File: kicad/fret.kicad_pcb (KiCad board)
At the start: 2 copper layers, 40 parts, among them J1 +5V, J10 CONN_01X06, J2 GNDPWR, J3 +3.3V, J4 GND, J5 SDA, J6 SCL, J7 TEST, J8 ~RST, P0 TOUCH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

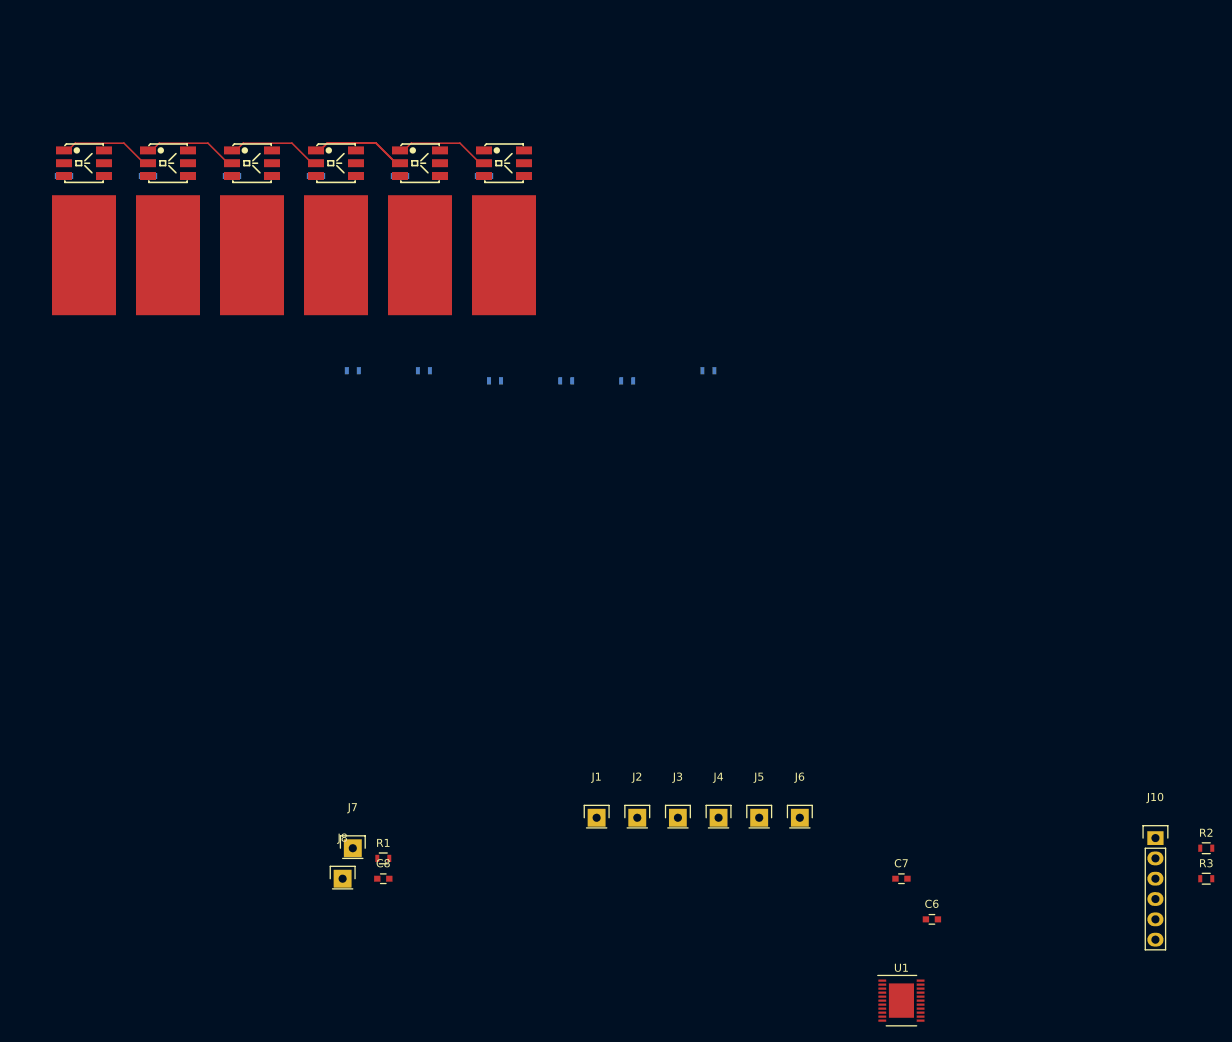
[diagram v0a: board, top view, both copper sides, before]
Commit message: kicad: almost finished layout with the msp430
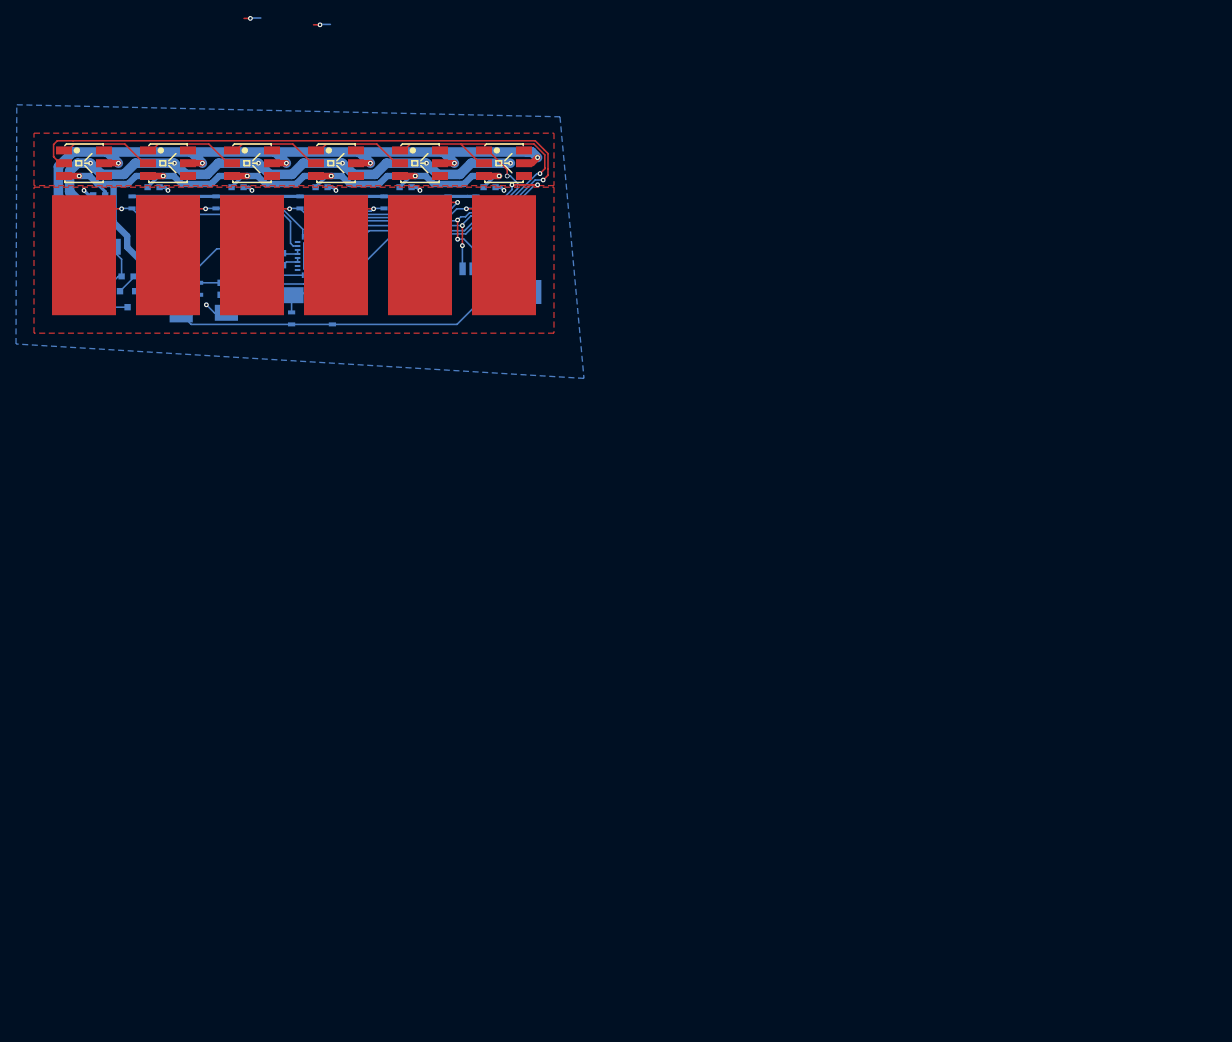
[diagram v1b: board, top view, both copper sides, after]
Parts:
- added C10: 22uF, Capacitors_SMD:C_0805, B.Cu at (44.7, 50.8)
- added C9: 22uF, Capacitors_SMD:C_0805, B.Cu at (38.7, 50.8)
- added JP1: GNDPWR-GND, Capacitors_SMD:C_0603, B.Cu at (41.7, 47.9)
- added U2: AP2210N-3.3TRG1, Housings_SOT-23_SOT-143_TSOT-6:SOT-23, B.Cu at (41.7, 50.8)
- C6, C7, C8, R1, R2, R3: moved to B.Cu
- J1, J2, J3, J4, J5, J6: footprint Pin_Headers:Pin_Header_Straight_1x01 -> guitar-components:IDC-1x1; moved to B.Cu
- J10: footprint Pin_Headers:Pin_Header_Straight_1x06 -> Connectors_Molex:Connector_Molex_PicoBlade_53261-0671; moved to B.Cu
- J7, J8: footprint Pin_Headers:Pin_Header_Straight_1x01 -> guitar-components:pad-2mm-round; moved to B.Cu
- U1: footprint Housings_DFN_QFN:DFN-22-1EP_5x6mm_Pitch0.5mm -> Housings_DFN_QFN:QFN-32-1EP_5x5mm_Pitch0.5mm; moved to B.Cu
- moved R2 132.1 mm to (62.2, 53.1), turned to 90 degrees
- moved R3 129.8 mm to (67.3, 53.1), turned to 90 degrees
- moved U1 118.3 mm to (65.3, 45.4), turned to 270 degrees
- moved C6 115.7 mm to (61.1, 45.8), turned to 270 degrees
- moved C7 110.5 mm to (59.5, 45.8), turned to 270 degrees
- moved J10 107.8 mm to (86.7, 49.9), turned to 180 degrees
- moved J2 97.2 mm to (39.4, 44.2)
- moved J1 96.8 mm to (35.0, 44.2)
- moved J3 88.4 mm to (48.4, 52.6)
- moved J4 88.1 mm to (54.0, 52.5)
- moved J6 87.7 mm to (67.2, 50.2)
- moved J5 87.6 mm to (62.2, 50.2)
- moved C8 76.5 mm to (53.3, 49.5), turned to 270 degrees
- moved J8 75.5 mm to (55.3, 48.9)
- moved R1 74.8 mm to (50.7, 49.5), turned to 270 degrees
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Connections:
- U1 pad 10: /LED6 -> /BUTTON
- U1 pad 13: Net-(U1-Pad13) -> /LED0
- U1 pad 14: /BUTTON -> Net-(U1-Pad14)
- U1 pad 9: /LED0 -> /LED6
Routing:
- net +3V3: track 0.00 -> 171.8 mm, vias 0 -> 6
- net +5V: track 0.00 -> 104.8 mm, vias 0 -> 6
- net /LED0: track 0.00 -> 99.3 mm, vias 0 -> 1
- net /CAOUT: track 0.00 -> 85.0 mm, vias 0 -> 2
- net GNDPWR: track 0.00 -> 80.2 mm, vias 0 -> 6
- net /BUTTON: track 11.9 -> 60.2 mm, vias 0 -> 3
- net /LED6: track 0.00 -> 39.8 mm, vias 0 -> 3
- net Net-(P4-Pad1): track 0.00 -> 32.1 mm, vias 0 -> 1
- net Net-(P5-Pad1): track 0.00 -> 30.4 mm, vias 0 -> 1
- net Net-(P0-Pad1): track 0.00 -> 26.4 mm, vias 0 -> 1
- net GND: track 0.00 -> 17.0 mm, vias 0 -> 7
- net Net-(P1-Pad1): track 0.00 -> 15.0 mm, vias 0 -> 1
- net /~RST: track 0.00 -> 14.4 mm
- net Net-(P3-Pad1): track 0.00 -> 12.3 mm, vias 0 -> 1
- net /LED4: track 23.8 -> 12.3 mm
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- added copper zone on B.Cu, net GND
- added copper zone on F.Cu, net GND
- added copper zone on F.Cu, net GNDPWR

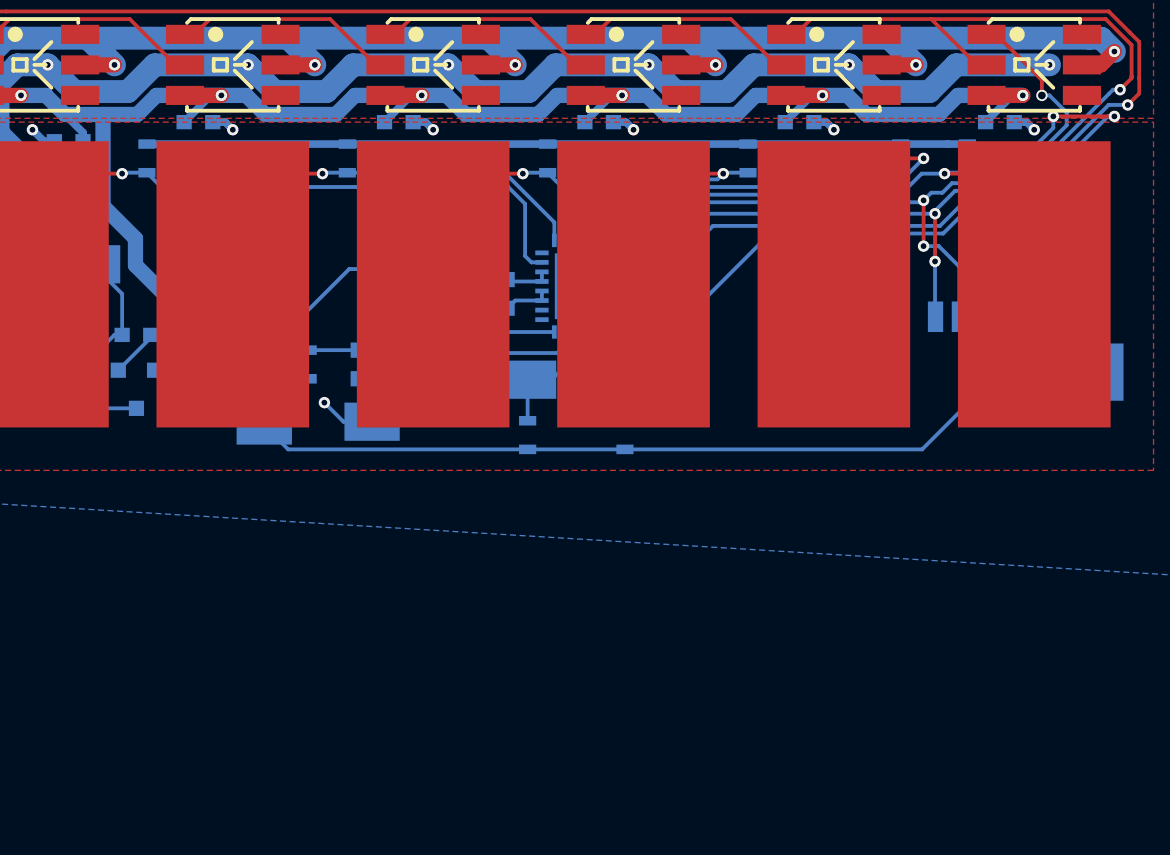
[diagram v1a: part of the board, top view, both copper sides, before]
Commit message: kicad: started fret layout with stm32
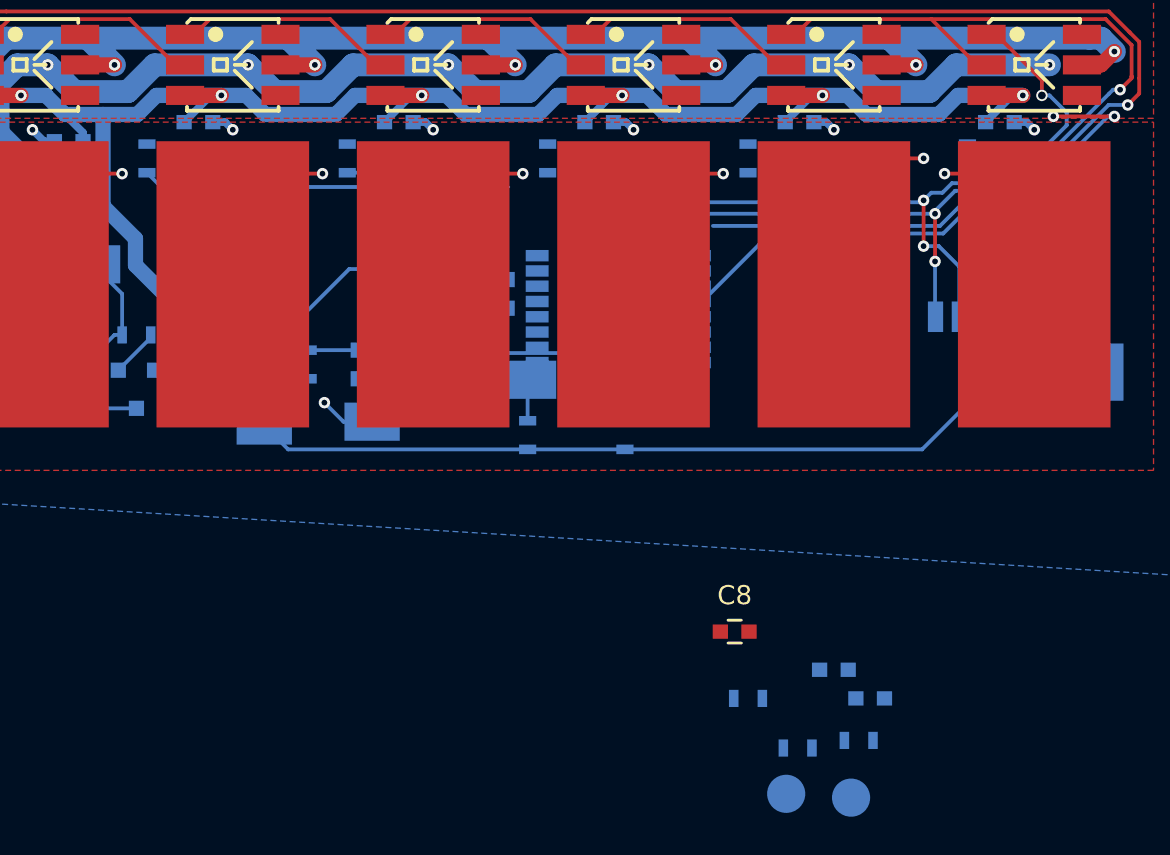
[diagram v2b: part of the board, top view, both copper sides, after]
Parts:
- added C12: 47nF, Capacitors_SMD:C_0603, B.Cu at (80.2, 67.0)
- added C13: 47nF, Capacitors_SMD:C_0603, B.Cu at (78.2, 65.5)
- added C8: 100nF, Capacitors_SMD:C_0603, F.Cu at (73.0, 63.5)
- added J11: SWCLK, guitar-components:pad-2mm-round, B.Cu at (75.8, 72.0)
- added J9: SWDIO, guitar-components:pad-2mm-round, B.Cu at (79.2, 72.2)
- added JP2: SCK-CONNECTION, Resistors_SMD:R_0603, B.Cu at (76.3, 69.5)
- added JP3: SPI-CONNECTION, Resistors_SMD:R_0603, B.Cu at (73.8, 67.0)
- added R12: 10k, Resistors_SMD:R_0603, B.Cu at (79.5, 69.2)
- C11: renamed from C8; value 1nF -> 100nF
- C6: value 1uF -> 100nF
- J7: value TEST -> BOOT0
- J8: value ~RST -> NRST
- JP1: footprint Capacitors_SMD:C_0603 -> Resistors_SMD:R_0603
- R0: renamed from R4; value 47k -> 10k
- R1: renamed from R5; value 47k -> 10k
- R2: renamed from R6; value 47k -> 10k
- R3: renamed from R7; value 47k -> 10k
- R4: renamed from R8; value 47k -> 10k
- R5: renamed from R9; value 47k -> 10k
- U1: value MSP430G2553IRHB32 -> STM32F051K*T; footprint Housings_DFN_QFN:QFN-32-1EP_5x5mm_Pitch0.5mm -> Housings_QFP:LQFP-32_7x7mm_Pitch0.8mm
- moved U1 2.00 mm to (67.0, 46.5), turned to 0 degrees
- moved R4 0.90 mm to (80.8, 38.6), turned to 0 degrees
- renumbered R1 to R6, R2 to R7, R3 to R8
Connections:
- C11 pad 1: /~RST -> /NRST
- J7 pad 1: /TEST -> /BOOT0
- J8 pad 1: /~RST -> /NRST
- R0 pad 1: Net-(P0-Pad1) -> Net-(R0-Pad1)
- R0 pad 2: /CAOUT -> Net-(P0-Pad1)
- R1 pad 1: Net-(P1-Pad1) -> Net-(R1-Pad1)
- R1 pad 2: /CAOUT -> Net-(P1-Pad1)
- R2 pad 1: Net-(P2-Pad1) -> Net-(R2-Pad1)
- R2 pad 2: /CAOUT -> Net-(P2-Pad1)
- R3 pad 1: Net-(P3-Pad1) -> Net-(R3-Pad1)
- R3 pad 2: /CAOUT -> Net-(P3-Pad1)
- R4 pad 1: Net-(P4-Pad1) -> Net-(R4-Pad1)
- R4 pad 2: /CAOUT -> Net-(P4-Pad1)
- R5 pad 1: Net-(P5-Pad1) -> Net-(R5-Pad1)
- R5 pad 2: /CAOUT -> Net-(P5-Pad1)
- R6 pad 1: /~RST -> /NRST
- U1 pad 1: Net-(P1-Pad1) -> +3V3
- U1 pad 10: /BUTTON -> Net-(U1-Pad10)
- U1 pad 11: Net-(U1-Pad11) -> /LED6
- U1 pad 12: Net-(U1-Pad12) -> /BUTTON
- U1 pad 16: Net-(U1-Pad16) -> GND
- U1 pad 17: Net-(U1-Pad17) -> +3V3
- U1 pad 19: Net-(U1-Pad19) -> Net-(R3-Pad1)
- U1 pad 2: Net-(P2-Pad1) -> Net-(U1-Pad2)
- U1 pad 20: /CAOUT -> Net-(R4-Pad1)
- U1 pad 21: /SCL -> Net-(R5-Pad1)
- U1 pad 22: /SDA -> Net-(C13-Pad1)
- U1 pad 23: /~RST -> Net-(U1-Pad23)
- U1 pad 24: /TEST -> /SWCLK
- U1 pad 25: Net-(U1-Pad25) -> /SWDIO
- U1 pad 26: Net-(U1-Pad26) -> /SCK
- U1 pad 27: GND -> /MISO
- U1 pad 28: GND -> /MISO
- U1 pad 29: +3V3 -> /SCL
- U1 pad 3: Net-(P3-Pad1) -> Net-(U1-Pad3)
- U1 pad 30: +3V3 -> /SDA
- U1 pad 31: Net-(P0-Pad1) -> /BOOT0
- U1 pad 32: (no net) -> GND
- U1 pad 4: Net-(P4-Pad1) -> /NRST
- U1 pad 5: Net-(P5-Pad1) -> +3V3
- U1 pad 6: Net-(U1-Pad6) -> Net-(R0-Pad1)
- U1 pad 7: Net-(U1-Pad7) -> Net-(R1-Pad1)
- U1 pad 8: (no net) -> Net-(R2-Pad1)
- U1 pad 9: /LED6 -> Net-(C12-Pad1)
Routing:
- net /CAOUT: track 85.0 -> 0.00 mm, vias 2 -> 0
- net (no net): track 4.24 -> 39.5 mm, vias 2 -> 4
- net Net-(P0-Pad1): track 26.4 -> 0.80 mm
- net Net-(P5-Pad1): track 30.4 -> 8.46 mm
- net Net-(P4-Pad1): track 32.1 -> 11.6 mm
- net Net-(R0-Pad1): track 0.00 -> 19.2 mm
- net /~RST: track 14.4 -> 0.00 mm
- net Net-(P1-Pad1): track 15.0 -> 0.80 mm
- net /NRST: track 0.00 -> 13.2 mm
- net Net-(P3-Pad1): track 12.3 -> 0.80 mm
- net /TEST: track 8.88 -> 0.00 mm
- net Net-(R1-Pad1): track 0.00 -> 8.25 mm
- net /LED0: track 99.3 -> 93.7 mm
- net Net-(P2-Pad1): track 6.02 -> 0.80 mm
- net /LED6: track 39.8 -> 35.1 mm
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
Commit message: kicad: layout was almost finished a while ago
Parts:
- removed the JP2 at (76.3, 69.5)
- C8: moved to B.Cu
- moved C12 32.8 mm to (63.2, 38.9), turned to 90 degrees
- moved R7 25.2 mm to (85.2, 43.0), turned to 270 degrees
- moved R12 23.6 mm to (62.5, 52.8), turned to 180 degrees
- moved J11 22.0 mm to (73.8, 50.0)
- moved C8 21.0 mm to (73.0, 42.5), turned to 90 degrees
- moved J9 20.2 mm to (73.8, 52.6)
- moved R8 19.2 mm to (83.5, 43.0), turned to 270 degrees
- moved C13 18.2 mm to (74.2, 47.8)
- moved J6 16.8 mm to (83.8, 47.5)
- moved J5 16.6 mm to (78.7, 47.5)
- moved JP2 15.9 mm to (66.5, 52.8), turned to 180 degrees
- moved R6 8.64 mm to (59.1, 47.6), turned to 0 degrees
- moved J7 6.96 mm to (58.2, 52.6)
- moved C11 6.77 mm to (59.1, 46.0), turned to 180 degrees
- moved J10 6.06 mm to (90.7, 45.2), turned to 270 degrees
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- renumbered JP3 to JP2
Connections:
- net Net-(C12-Pad1) renamed /CG1
- net Net-(C13-Pad1) renamed /CG4
- net Net-(R0-Pad1) renamed /P0
- net Net-(R1-Pad1) renamed /P1
- net Net-(R2-Pad1) renamed /P2
- net Net-(R3-Pad1) renamed /P3
- net Net-(R4-Pad1) renamed /P4
- net Net-(R5-Pad1) renamed /P5
- J10 pad 3: /SCL -> /SCK
- J6 pad 1: /SCL -> /SCK
- R8 pad 2: /SCL -> /SCK
- U1 pad 29: /SCL -> /SCK
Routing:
- net GND: track 14.5 -> 257.3 mm, vias 7 -> 22
- net /LED0: track 93.7 -> 51.6 mm
- net (no net): track 39.5 -> 0.00 mm, vias 4 -> 0
- net /SCK: track 0.00 -> 34.0 mm
- net /SDA: track 5.54 -> 29.7 mm
- net +3V3: track 169.6 -> 145.5 mm, vias 6 -> 7
- net /BUTTON: track 55.6 -> 75.4 mm, vias 3 -> 1
- net /LED6: track 35.1 -> 50.5 mm, vias 3 -> 2
- net /P4: track 0.00 -> 11.7 mm
- net /P5: track 0.00 -> 11.3 mm
- net /BOOT0: track 1.98 -> 9.65 mm
- net /P3: track 0.00 -> 6.46 mm
- net /SWDIO: track 0.00 -> 4.77 mm
- net /MISO: track 0.00 -> 4.54 mm
- net /P2: track 0.00 -> 4.36 mm
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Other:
- board text added: "Link TP Connector"
- board text added: "MIDI Guitar Fret - v2.0 - Spring 2015 - Alexandru Stan"

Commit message: kicad: Ordered fret board
Board modifications:
* SWDIO now in the right spot
* Silkscreen adjustments
* Testing touchpad silkscreen edge effects on the backend

Board is v2.0

Sent order to elecrow.
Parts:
- moved J9 2.60 mm to (73.8, 50.0)
- moved J11 2.60 mm to (76.3, 50.0)
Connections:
- U1 pad 23: Net-(U1-Pad23) -> /SWDIO
- U1 pad 25: /SWDIO -> Net-(U1-Pad25)
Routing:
- net (no net): track 0.00 -> 114.5 mm
- net /SWCLK: track 2.84 -> 6.89 mm
- net GND: track 257.3 -> 254.5 mm, vias 22 -> 21
- net /SDA: track 29.7 -> 31.5 mm
- net /SWDIO: track 4.77 -> 4.16 mm
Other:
- board text added: "MIDI Guitar Fret - v2.0 - Spring 2015 - Alexandru M. Stan"
- board text removed: "MIDI Guitar Fret - v2.0 - Spring 2015 - Alexandru Stan"
